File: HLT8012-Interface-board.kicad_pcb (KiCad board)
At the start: 2 copper layers, 33 x 32.5 mm, 18 parts, among them J1 +(ev), J2 -(ev), J3 LOAD, J4 DC, U1 HLW8012

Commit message: feat: update
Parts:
- added J5: Conn_01x03_Pin, Connector_PinHeader_2.00mm:PinHeader_1x03_P2.00mm_Vertical, F.Cu at (112.5, 135.1)
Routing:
- net CF: track 0.00 -> 20.5 mm, vias 0 -> 1
- net CF1: track 0.00 -> 19.2 mm
- net SEL: track 0.00 -> 16.7 mm, vias 0 -> 1
- net -AC: track 13.8 -> 14.9 mm
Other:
- outline, holes or cut-outs redrawn

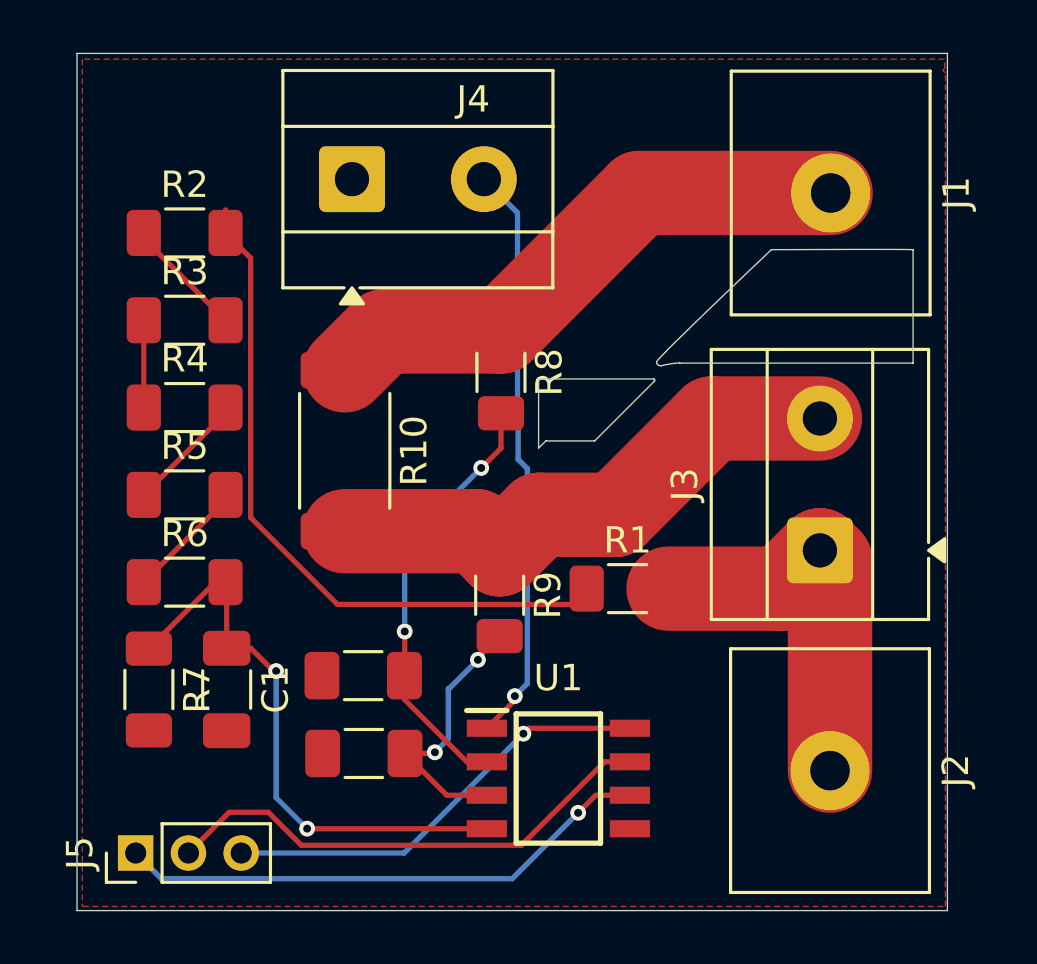
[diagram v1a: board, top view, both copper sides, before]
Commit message: feat: added thermal relief
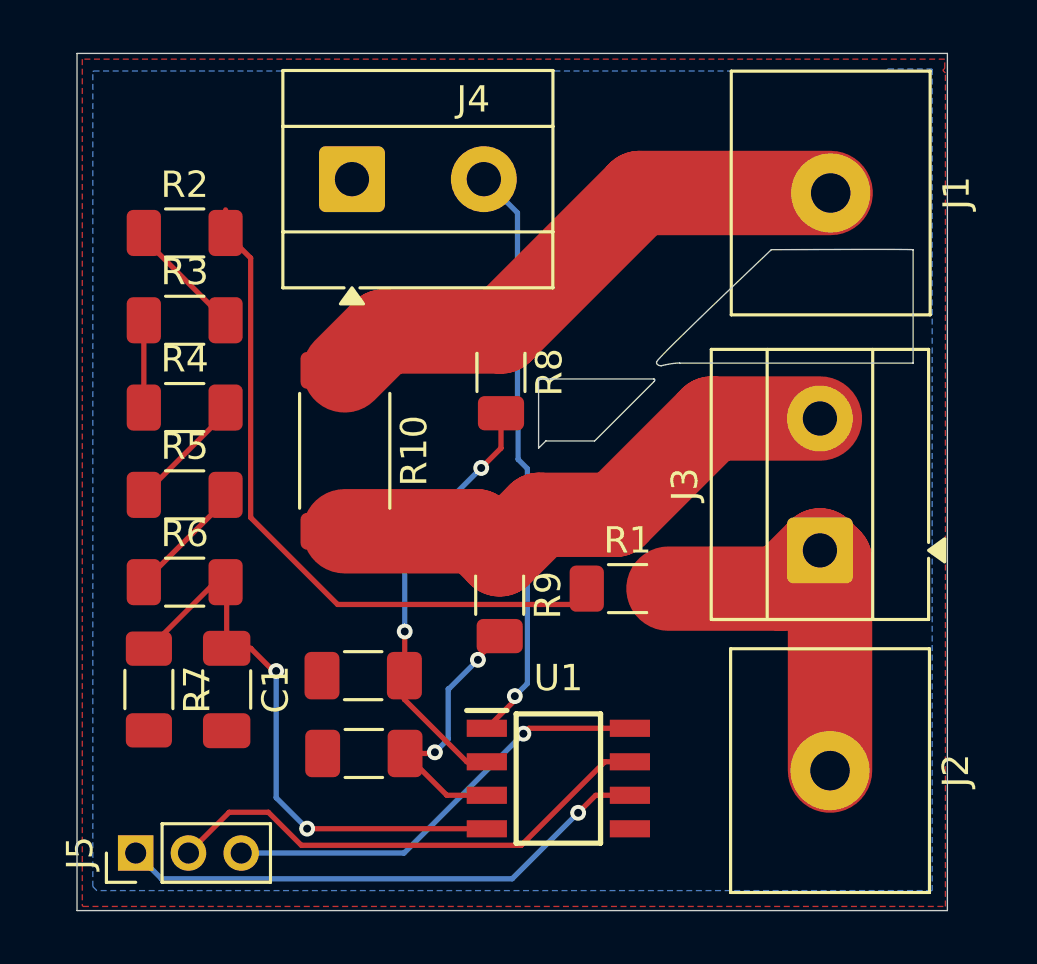
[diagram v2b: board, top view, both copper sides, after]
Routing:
- added copper zone on B.Cu, net GND
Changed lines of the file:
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@@
 		(filled_areas_thickness no)
 		(fill yes
+			(mode hatch)
 			(thermal_gap 0.5)
 			(thermal_bridge_width 0.5)
+			(hatch_thickness 1)
+			(hatch_gap 1.5)
+			(hatch_orientation 0)
+			(hatch_border_algorithm hatch_thickness)
+			(hatch_min_hole_area 0.3)
 		)
 		(polygon
@@
 			)
 		)
+	)
+	(zone
+		(net 2)
+		(net_name "GND")
+		(layer "B.Cu")
+		(hatch edge 0.5)
+		(priority 1)
+		(connect_pads
+			(clearance 0.5)
+		)
+		(min_thickness 0.25)
+		(filled_areas_thickness no)
+		(fill yes
+			(mode hatch)
+			(thermal_gap 0.5)
+			(thermal_bridge_width 0.5)
+			(hatch_thickness 1)
+			(hatch_gap 1.5)
+			(hatch_orientation 0)
+			(hatch_border_algorithm hatch_thickness)
+			(hatch_min_hole_area 0.3)
+		)
+		(polygon
+			(pts
+				(xy 142.65 105.35) (xy 142.65 136.5) (xy 110.975 136.5) (xy 110.825 136.35) (xy 110.825 105.45)
+				(xy 110.85 105.425) (xy 140.9 105.425) (xy 140.975 105.35)
+			)
+		)
